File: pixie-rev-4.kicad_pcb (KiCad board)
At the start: 4 copper layers, 40 x 30 mm, 42 parts, among them J1 THD_FPC_24, SW1 SW_tact_52x52, SW2 SW_tact_52x52, SW3 SW_tact_52x52, SW4 SW_tact_52x52, U1 USBLC6-2SC6, U2 W25Q128JVS, U3 SPX3819M5-L-3-3, U4 ESP32_C3, Y2 Crystal_GND24

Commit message: Check-in before trying ESP32-C3-F4.
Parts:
- U4: footprint Package_DFN_QFN:HVQFN-32-1EP_5x5mm_P0.5mm_EP3.1x3.1mm -> Package_DFN_QFN:QFN-32-1EP_5x5mm_P0.5mm_EP3.7x3.7mm
- moved C16 1.17 mm to (152.5, 54.3)
- moved C12 0.78 mm to (154.8, 63.5)
- moved C15 0.78 mm to (154.8, 62.8)
- moved L1 0.78 mm to (156.0, 63.1)
- moved C10 0.77 mm to (156.8, 63.1)
- moved C11 0.47 mm to (152.8, 62.0)
- moved C14 0.47 mm to (152.4, 63.2)
- moved L2 0.47 mm to (153.2, 63.2)
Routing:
- net GND: track 38.5 -> 40.7 mm, vias 30 -> 64
- net Net-(U4-XTAL_N): track 8.19 -> 8.91 mm
- net Net-(AE1-Pad1): track 2.35 -> 1.83 mm
- added copper zone on F.Cu, net GND

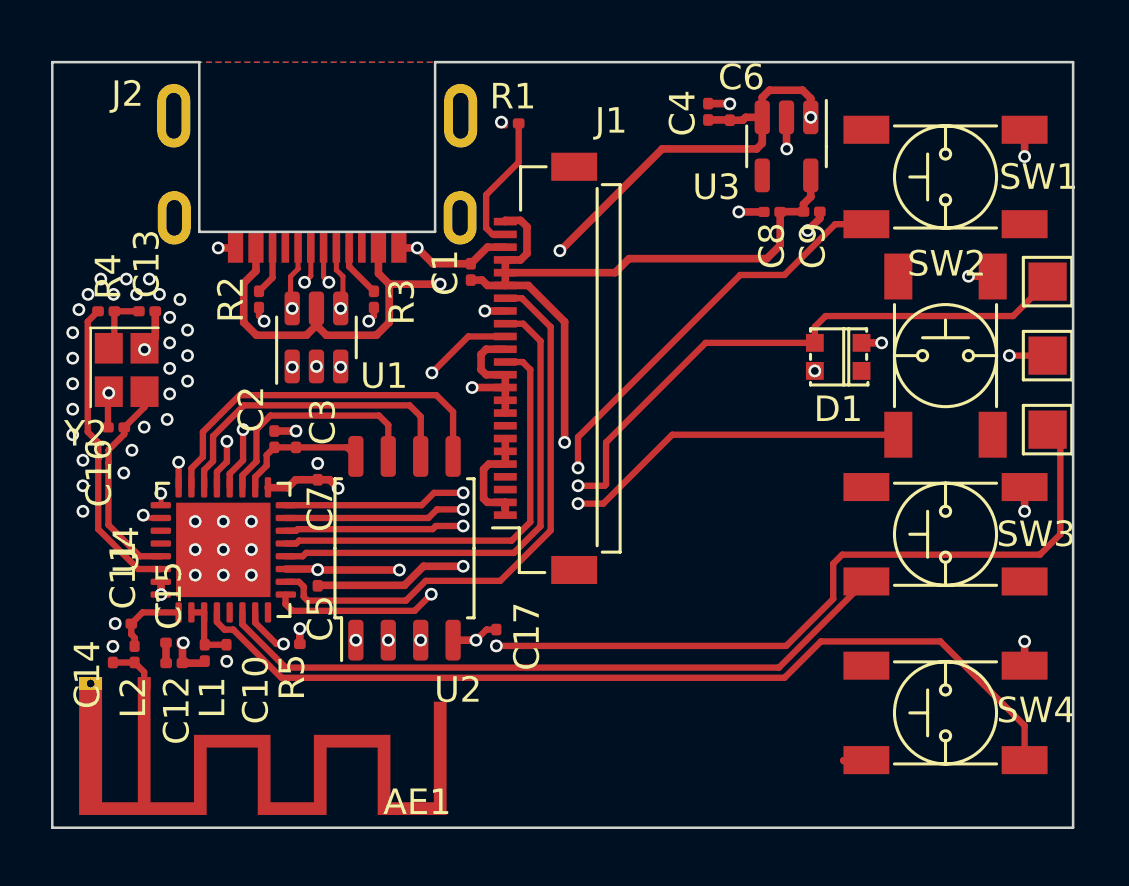
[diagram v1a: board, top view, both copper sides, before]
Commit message: Checking in before updating against ESP32-C3-WROOM-02 designs.
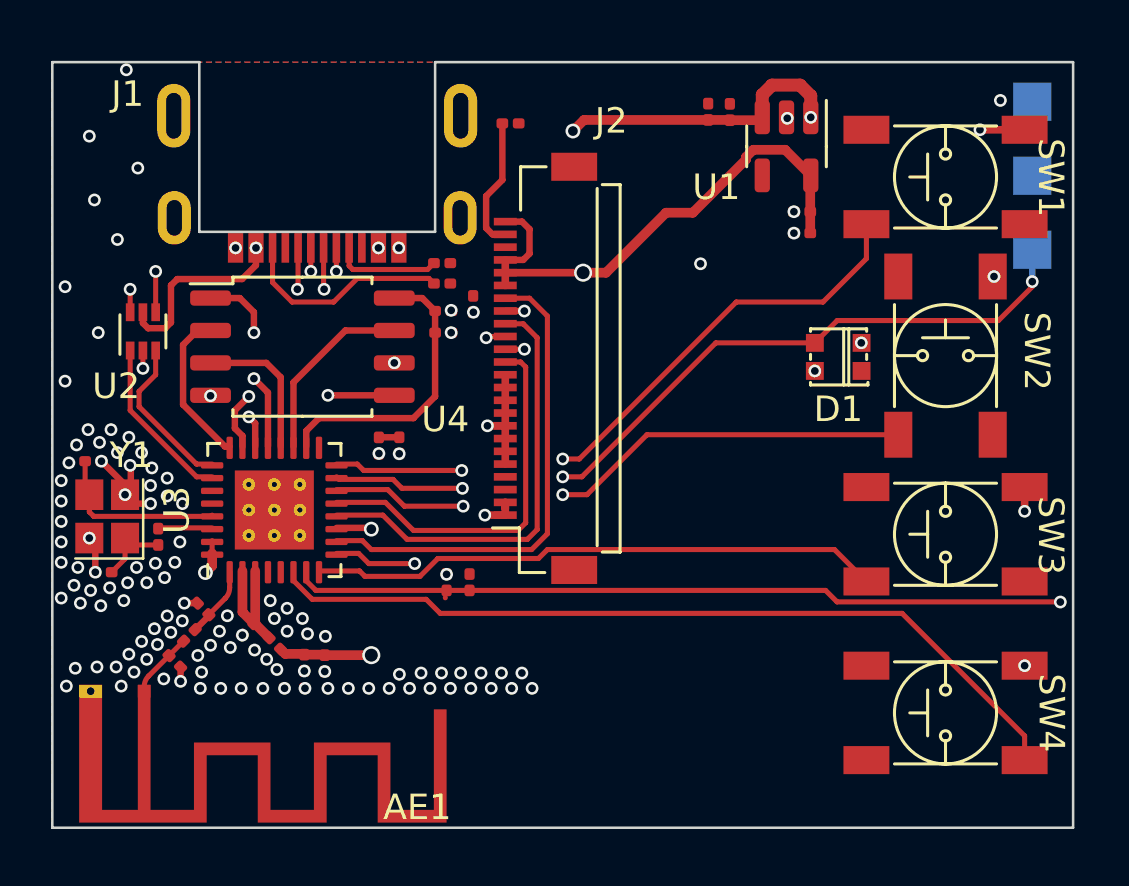
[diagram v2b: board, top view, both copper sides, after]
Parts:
- removed the C2 at (158.7, 54.8)
- removed the C3 at (159.6, 54.8)
- removed the U1 at (160.3, 50.8)
- added C16: 100n, Capacitor_SMD:C_0201_0603Metric, F.Cu at (165.3, 50.6)
- added C17: 10u, Capacitor_SMD:C_0201_0603Metric, F.Cu at (165.3, 49.8)
- added U3: ESP32-C3, Package_DFN_QFN:QFN-32-1EP_5x5mm_P0.5mm_EP3.1x3.1mm_ThermalVias, F.Cu at (158.7, 57.5)
- BOOT1, GND1, PU1: moved to B.Cu
- U2: value W25Q128JVS -> USBLC6-2SC6; footprint Package_SO:SOIC-8_5.23x5.23mm_P1.27mm -> Package_TO_SOT_SMD:SOT-563
- U4: value ESP32_C3 -> W25Q128JVS; footprint Package_DFN_QFN:QFN-32-1EP_5x5mm_P0.5mm_EP3.7x3.7mm -> Package_SO:SOIC-8_5.23x5.23mm_P1.27mm
- moved U2 13.3 mm to (153.6, 50.5)
- moved PU1 12.9 mm to (188.4, 41.5)
- moved C14 10.4 mm to (152.0, 60.0), turned to 180 degrees
- moved R5 9.07 mm to (154.2, 58.6), turned to -90 degrees
- moved U4 8.54 mm to (159.8, 51.1), turned to 0 degrees
- moved R2 7.38 mm to (166.3, 60.4), turned to 90 degrees
- moved R1 7.20 mm to (165.3, 48.7), turned to 180 degrees
- moved GND1 7.08 mm to (188.4, 44.5)
- moved C2 6.09 mm to (163.6, 55.0)
- moved C15 5.96 mm to (160.7, 63.6), turned to -90 degrees
- moved Y1 5.79 mm to (152.2, 57.8), turned to 90 degrees
- moved C13 5.10 mm to (159.9, 63.5), turned to -90 degrees
- moved C9 3.19 mm to (155.9, 61.4), turned to 135 degrees
- moved R3 3.03 mm to (165.3, 47.9), turned to 180 degrees
- moved C6 2.92 mm to (165.4, 60.4)
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- renumbered C4 to C1, C16 to C11, C14 to C12, C12 to C13, C13 to C14, C5 to C2, C6 to C3, C7 to C4, C8 to C5, C17 to C6, C9 to C7, C1 to C8, C11 to C9, J2 to J1, J1 to J2, L2 to L1, L1 to L2, R2 to R1, R5 to R2, R1 to R4, R4 to R5, U3 to U1, Y2 to Y1
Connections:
- C11 pad 1: Net-(U4-XTAL_N) -> /XTAL_N
- C9 pad 1: Net-(U4-LNA_IN) -> /ANTENNA
- L1 pad 1: Net-(U4-LNA_IN) -> /ANTENNA
- R5 pad 1: Net-(U4-XTAL_P) -> /XTAL_P
- U2 pad 1: Net-(U2-~{CS}) -> /MCU_USB_P
- U2 pad 2: Net-(U2-DO(IO1)) -> GND
- U2 pad 3: Net-(U2-IO2) -> /MCU_USB_N
- U2 pad 4: GND -> /USB_D-
- U2 pad 5: Net-(U2-DI(IO0)) -> /VBUS
- U2 pad 6: Net-(U2-CLK) -> /USB_D+
- U4 pad 1: Net-(U4-LNA_IN) -> /SPI_CS0
- U4 pad 2: /VRF -> /SPI_Q
- U4 pad 3: /VRF -> /SPI_WP
- U4 pad 4: /SW_4 -> GND
- U4 pad 5: unconnected-(U4-XTAL_32K_N_IO1-Pad5) -> /SPI_D
- U4 pad 6: /SW_3 -> /SPI_CLK
- U4 pad 7: /CHIP_PU -> /SPI_HD
- U4 pad 8: unconnected-(U4-IO3-Pad8) -> /VCC_SPI
- Y1 pad 3: Net-(U4-XTAL_N) -> /XTAL_N
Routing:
- net GND: track 40.7 -> 17.9 mm, vias 64 -> 130
- net Net-(U2-DI(IO0)): track 14.8 -> 0.00 mm
- net Net-(U2-IO2): track 13.6 -> 0.00 mm, vias 2 -> 0
- net Net-(U2-DO(IO1)): track 12.9 -> 0.00 mm, vias 2 -> 0
- net Net-(U2-CLK): track 12.5 -> 0.00 mm
- net Net-(U2-~{CS}): track 12.0 -> 0.00 mm, vias 2 -> 0
- net Net-(U4-XTAL_P): track 12.0 -> 0.00 mm
- net /CHIP_PU: track 39.5 -> 51.4 mm
- net /VCC_SPI: track 0.00 -> 11.4 mm
- net Net-(U2-IO3): track 9.28 -> 0.00 mm
- net Net-(U4-XTAL_N): track 8.91 -> 0.00 mm
- net /SPI_D: track 0.00 -> 8.03 mm, vias 0 -> 2
- net /SPI_CLK: track 0.00 -> 7.85 mm, vias 0 -> 2
- net /SPI_CS0: track 0.00 -> 7.42 mm, vias 0 -> 2
- net /SPI_HD: track 0.00 -> 7.31 mm
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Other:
- board text added: "BOOT"
- board text added: "GND"
- board text added: "RESET"
- board text added: "rev.3"
- board text removed: "rev-4u1"

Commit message: JLCPCB Submit
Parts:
- removed AE1: PCB_ANTENNA, RF_Antenna:Texas_SWRA117D_2.4GHz_Left
- removed BOOT1, GND1, PU1: TestPoint, TestPoint:TestPoint_Pad_1.5x1.5mm
- removed C1, C15, C17, C2, C7: 10u, Capacitor_SMD:C_0201_0603Metric
- removed C10, C13, C16, C3, C4, C5, C6, C8: 100n, Capacitor_SMD:C_0201_0603Metric
- removed C11, C14: 10p, Capacitor_SMD:C_0201_0603Metric
- removed C12, C9: 3p3, Capacitor_SMD:C_0201_0603Metric
- removed D1: WS2812B, firefly:WS2812B
- removed J1: ~, firefly:USB_C_SINK
- removed J2: THD_FPC_24, firefly:THD_FPC_24
- removed L1, L2: 2n2, Inductor_SMD:L_0201_0603Metric
- removed R1: 5K1 (1%), Resistor_SMD:R_0201_0603Metric
- removed R2: 5k1, Resistor_SMD:R_0201_0603Metric
- removed R3: 5k1 (1%), Resistor_SMD:R_0201_0603Metric
- removed R4: 10R, Resistor_SMD:R_0201_0603Metric
- removed R5: 22R, Resistor_SMD:R_0201_0603Metric
- removed SW1, SW2, SW3, SW4: SW_tact_52x52, firefly:SW_tact_52x52
- removed U1: SPX3819M5-L-3-3, Package_TO_SOT_SMD:SOT-23-5
- removed U2: USBLC6-2SC6, Package_TO_SOT_SMD:SOT-563
- removed U3: ESP32-C3, Package_DFN_QFN:QFN-32-1EP_5x5mm_P0.5mm_EP3.1x3.1mm_ThermalVias
- removed U4: W25Q128JVS, Package_SO:SOIC-8_5.23x5.23mm_P1.27mm
- removed Y1: Crystal_GND24, firefly:Crystal_SeikoEpson_FA20H
- added AE301: PCB_ANTENNA, firefly:PCB_Antenna, F.Cu at (153.6, 64.5)
- added BOOT301: TestPoint, TestPoint:TestPoint_Pad_1.5x1.5mm, B.Cu at (187.8, 42.2)
- added C201: 10u, Capacitor_SMD:C_0402_1005Metric, F.Cu at (176.2, 41.6)
- added C202: 100n, Capacitor_SMD:C_0201_0603Metric, F.Cu at (176.4, 42.5)
- added C203: 100n, Capacitor_SMD:C_0201_0603Metric, F.Cu at (178.3, 46.0)
- added C204: 10u, Capacitor_SMD:C_0402_1005Metric, F.Cu at (179.7, 45.8)
- added C301: 3p3, Capacitor_SMD:C_0201_0603Metric, F.Cu at (155.7, 60.2)
- added C302: 10p, Capacitor_SMD:C_0201_0603Metric, F.Cu at (151.9, 54.5)
- added C303: 100n, Capacitor_SMD:C_0201_0603Metric, F.Cu at (168.2, 61.4)
- added C304: 3p3, Capacitor_SMD:C_0201_0603Metric, F.Cu at (156.3, 62.4)
- added C305: 10p, Capacitor_SMD:C_0201_0603Metric, F.Cu at (152.3, 58.9)
- added C306: 1u, Capacitor_SMD:C_0201_0603Metric, F.Cu at (162.3, 51.0)
- added C307: 100n, Capacitor_SMD:C_0201_0603Metric, F.Cu at (157.2, 60.5)
- added C308: 1u, Capacitor_SMD:C_0201_0603Metric, F.Cu at (153.9, 59.5)
- added C309: 100n, Capacitor_SMD:C_0201_0603Metric, F.Cu at (159.7, 61.7)
- added C310: 10n, Capacitor_SMD:C_0201_0603Metric, F.Cu at (153.4, 60.3)
- added C311: 100n, Capacitor_SMD:C_0201_0603Metric, F.Cu at (160.2, 60.5)
- added C312: 100n, Capacitor_SMD:C_0201_0603Metric, F.Cu at (160.6, 52.3)
- added C313: 10u, Capacitor_SMD:C_0402_1005Metric, F.Cu at (160.6, 61.9)
- added C401: 100n, Capacitor_SMD:C_0201_0603Metric, F.Cu at (166.4, 48.6)
- added D401: WS2812B, firefly:WS2812B, F.Cu at (180.9, 52.2)
- added GND201: TestPoint, TestPoint:TestPoint_Pad_1.5x1.5mm, B.Cu at (187.7, 44.9)
- added J401: ~, firefly:THD_FPC_24, F.Cu at (169.0, 52.0)
- added L301: 2n2, Inductor_SMD:L_0201_0603Metric, F.Cu at (156.0, 61.3)
- added L302: 2n2, Inductor_SMD:L_0201_0603Metric, F.Cu at (158.2, 61.0)
- added PU301: TestPoint, TestPoint:TestPoint_Pad_1.5x1.5mm, B.Cu at (187.8, 47.5)
- added R201: 5K1, Resistor_SMD:R_0201_0603Metric, F.Cu at (155.4, 49.1)
- added R202: 5k1, Resistor_SMD:R_0201_0603Metric, F.Cu at (163.4, 49.2)
- added R301: 5k1, Resistor_SMD:R_0201_0603Metric, F.Cu at (166.6, 61.4)
- added R302: 22R, Resistor_SMD:R_0201_0603Metric, F.Cu at (154.2, 57.6)
- added R303: 0R, Resistor_SMD:R_0201_0603Metric, F.Cu at (158.0, 51.5)
- added R304: 100R, Resistor_SMD:R_0201_0603Metric, F.Cu at (157.2, 51.5)
- added R305: 100R, Resistor_SMD:R_0201_0603Metric, F.Cu at (155.7, 51.5)
- added R306: 100R, Resistor_SMD:R_0201_0603Metric, F.Cu at (159.5, 51.5)
- added R307: 100R, Resistor_SMD:R_0201_0603Metric, F.Cu at (156.5, 51.5)
- added R308: 100R, Resistor_SMD:R_0201_0603Metric, F.Cu at (158.7, 51.5)
- added R401: 10R, Resistor_SMD:R_0201_0603Metric, F.Cu at (168.7, 42.6)
- added SW101: SW_tact_52x52, firefly:SW_tact_52x52, F.Cu at (185.0, 44.5)
- added SW102: SW_tact_52x52, firefly:SW_tact_52x52, F.Cu at (185.0, 51.5)
- added SW103: SW_tact_52x52, firefly:SW_tact_52x52, F.Cu at (185.0, 58.5)
- added SW104: SW_tact_52x52, firefly:SW_tact_52x52, F.Cu at (185.0, 65.5)
- added U201: USBLC6-2SC6, Package_TO_SOT_SMD:SOT-563, F.Cu at (153.5, 50.0)
- added U202: SPX3819M5-L-3-3, Package_TO_SOT_SMD:SOT-23-5, F.Cu at (179.0, 43.2)
- added U301: W25Q128JVS, Package_SO:SOIC-8_5.23x5.23mm_P1.27mm, F.Cu at (163.9, 56.2)
- added U302: ESP32-C3, Package_DFN_QFN:QFN-32-1EP_5x5mm_P0.5mm_EP3.1x3.1mm, F.Cu at (157.8, 56.5)
- added U401: SN74LVC1T45DBV, Package_TO_SOT_SMD:SOT-23-6, F.Cu at (180.2, 49.1)
- added Y301: 40Mhz, firefly:Crystal_SeikoEpson_FA20H, F.Cu at (152.2, 56.7)
- added locked: ~, firefly:USB_C_SINK, F.Cu at (160.4, 40.0)
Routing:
- net 3V3: track 0.00 -> 77.5 mm, vias 0 -> 5
- net /3V3: track 63.9 -> 0.00 mm, vias 4 -> 0
- net 5V: track 0.00 -> 59.3 mm, vias 0 -> 5
- net /CHIP_PU: track 51.4 -> 0.00 mm, vias 2 -> 0
- net /VBUS: track 45.4 -> 0.00 mm, vias 5 -> 0
- net /MCU/CHIP_PU: track 0.00 -> 38.5 mm, vias 0 -> 3
- net /MCU/DISP_RST: track 0.00 -> 19.8 mm
- net /MCU/DISP_DC: track 0.00 -> 19.2 mm, vias 0 -> 2
- net /DISP_RST: track 19.1 -> 0.00 mm
- net /MCU/DISP_SCL: track 0.00 -> 18.5 mm
- net /DISP_SCL: track 17.4 -> 0.00 mm
- net /DISP_SDA: track 15.0 -> 0.00 mm
- net /MCU/FLASH_IO1: track 0.00 -> 15.0 mm, vias 0 -> 2
- net /DISP_DC: track 14.0 -> 0.00 mm, vias 2 -> 0
- net /MCU/FLASH_IO2: track 0.00 -> 13.5 mm, vias 0 -> 2
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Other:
- board text added: "rev.4"
- board text removed: "rev.3"

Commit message: Checking in before submitting rev.5 to JLCPCB.
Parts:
- removed SW101, SW102, SW103, SW104: SW_tact_52x52, firefly:SW_tact_52x52
- added 3V1: TestPoint, TestPoint:TestPoint_Pad_1.0x1.0mm, F.Cu at (121.2, 93.0)
- added 5V1: TestPoint, TestPoint:TestPoint_Pad_1.0x1.0mm, F.Cu at (129.6, 93.0)
- added C19: 100n, Capacitor_SMD:C_0201_0603Metric, F.Cu at (125.9, 72.9)
- added C20: 100n, Capacitor_SMD:C_0201_0603Metric, F.Cu at (129.3, 74.5)
- added D2: WS2812B, firefly:WS2812B, F.Cu at (132.1, 81.5)
- added D3: WS2812B, firefly:WS2812B, F.Cu at (132.1, 88.5)
- added D4: WS2812B, firefly:WS2812B, F.Cu at (132.1, 95.5)
- added R11: 499R, Resistor_SMD:R_0201_0603Metric, F.Cu at (101.8, 81.1)
- added REF**: mouse-bite-3.5, firefly:mouse-bite-3.5, F.Cu at (100.7, 65.5)
- added REF**: mouse-bite-3.5, firefly:mouse-bite-3.5, F.Cu at (139.3, 75.5)
- added REF**: mouse-bite-3.5, firefly:mouse-bite-3.5, F.Cu at (100.7, 75.5)
- added REF**: fiducial, firefly:fiducial, F.Cu at (96.8, 129.2)
- added REF**: mouse-bite-3.5, firefly:mouse-bite-3.5, F.Cu at (158.8, 70.8)
- added REF**: fiducial, firefly:fiducial, F.Cu at (158.8, 129.2)
- added REF**: fiducial, firefly:fiducial, F.Cu at (96.8, 66.8)
- added REF**: mouse-bite-3.5, firefly:mouse-bite-3.5, F.Cu at (150.1, 99.2)
- added REF**: mouse-bite-3.5, firefly:mouse-bite-3.5, F.Cu at (100.7, 128.4)
- added REF**: mouse-bite-3.5, firefly:mouse-bite-3.5, F.Cu at (100.7, 104.5)
- added REF**: mouse-bite-3.5, firefly:mouse-bite-3.5, F.Cu at (145.9, 70.8)
- added REF**: mouse-bite-3.5, firefly:mouse-bite-3.5, F.Cu at (133.9, 70.7)
- added REF**: fiducial, firefly:fiducial, F.Cu at (158.8, 66.8)
- added REF**: mouse-bite-3.5, firefly:mouse-bite-3.5, F.Cu at (133.9, 99.3)
- added REF**: logo-pin-25-1, firefly:logo-pin-25-1, F.Cu at (149.5, 113.5)
- added SW1: ~, firefly:button-oval, F.Cu at (135.5, 74.5)
- added SW2: ~, firefly:button-oval, F.Cu at (135.5, 81.5)
- added SW3: ~, firefly:button-oval, F.Cu at (135.5, 88.5)
- added SW4: ~, firefly:button-oval, F.Cu at (135.5, 95.5)
- added TP1: TestPoint, TestPoint:TestPoint_Pad_D1.0mm, F.Cu at (102.5, 75.2)
- added TP2: TestPoint, TestPoint:TestPoint_Pad_D1.0mm, F.Cu at (102.4, 71.9)
- BOOT1: renamed from BOOT301; footprint TestPoint:TestPoint_Pad_1.5x1.5mm -> TestPoint:TestPoint_Pad_D1.0mm; moved to F.Cu
- GND1: renamed from GND201; footprint TestPoint:TestPoint_Pad_1.5x1.5mm -> TestPoint:TestPoint_Pad_1.0x1.0mm; moved to F.Cu
- PU1: renamed from PU301; footprint TestPoint:TestPoint_Pad_1.5x1.5mm -> TestPoint:TestPoint_Pad_D1.0mm; moved to F.Cu
- Y1: renamed from Y301; footprint firefly:Crystal_SeikoEpson_FA20H -> Crystal:Crystal_SMD_2520-4Pin_2.5x2.0mm
- moved PU1 85.9 mm to (114.7, 92.7), turned to 0 degrees
- moved GND1 74.2 mm to (118.4, 71.4), turned to 0 degrees
- moved C4 73.5 mm to (123.7, 93.4), turned to 90 degrees
- moved C3 73.1 mm to (122.8, 93.6), turned to 90 degrees
- moved U2 72.4 mm to (126.4, 93.0), turned to 180 degrees
- moved BOOT1 69.3 mm to (124.8, 71.4), turned to 0 degrees
- moved C2 69.0 mm to (126.7, 90.4), turned to 90 degrees
- moved C1 68.7 mm to (128.1, 90.7), turned to 0 degrees
- moved C7 63.7 mm to (112.9, 93.0), turned to 180 degrees
- moved R3 61.9 mm to (112.9, 92.2)
- moved U4 58.3 mm to (107.8, 86.5)
- moved C12 58.3 mm to (103.9, 89.5)
- moved C17 58.3 mm to (110.6, 91.9)
- moved C18 58.3 mm to (116.4, 78.6)
- moved C8 58.3 mm to (106.3, 92.4)
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- renumbered AE301 to AE1, C201 to C1, C306 to C10, C307 to C11, C308 to C12, C309 to C13, C310 to C14, C311 to C15, C312 to C16, C313 to C17, C401 to C18, C202 to C2, C203 to C3, C204 to C4, C301 to C5, C302 to C6, C303 to C7, C304 to C8, C305 to C9, D401 to D1, J401 to J2, L301 to L1, L302 to L2, R201 to R1, R308 to R10, R401 to R12, R202 to R2, R301 to R3, R302 to R4, R303 to R5, R304 to R6, R305 to R7, R306 to R8, R307 to R9, U201 to U1, U202 to U2, U301 to U3, U302 to U4, U401 to U5
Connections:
- D1 pad 1: unconnected-(D401-D0-Pad1) -> Net-(D1-D0)
- U4 pad 14: /SW_2 -> /MCU/SW_2
- U4 pad 16: /SW_1 -> /MCU/SW_1
- U4 pad 27: unconnected-(U302-U0RXD/GPIO20-Pad27) -> /MCU/IO20
- U4 pad 28: unconnected-(U302-U0TXD/GPIO21-Pad28) -> Net-(U4-U0TXD/GPIO21)
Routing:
- net /MCU/SW_1: track 0.00 -> 38.6 mm, vias 0 -> 2
- net /MCU/SW_2: track 0.00 -> 31.2 mm, vias 0 -> 2
- net /MCU/CHIP_PU: track 38.5 -> 10.9 mm, vias 3 -> 2
- net /SW_1: track 25.6 -> 0.00 mm, vias 2 -> 0
- net /SW_2: track 23.4 -> 0.00 mm, vias 2 -> 0
- net 5V: track 59.3 -> 79.9 mm, vias 5 -> 3
- net /MCU/IO20: track 0.00 -> 13.2 mm
- net /PIXEL: track 37.2 -> 26.4 mm, vias 3 -> 2
- net /MCU/IO21: track 0.00 -> 10.0 mm
- net Net-(U4-U0TXD/GPIO21): track 0.00 -> 6.63 mm, vias 0 -> 2
- net Net-(D2-D0): track 0.00 -> 5.63 mm
- net Net-(D3-D0): track 0.00 -> 5.63 mm
- net Net-(D1-D0): track 0.00 -> 5.63 mm
- net /SW_3: track 23.0 -> 28.2 mm
- net /MCU/DISP_DC: track 19.2 -> 15.4 mm
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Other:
- board size 40 x 30 mm -> 70 x 70 mm
- board text added: "1"
- board text added: "2"
- board text added: "20"
- board text added: "21"
- board text added: "3"
- board text added: "3V"
- board text added: "4"
- board text added: "5V"
- board text added: "B"
- board text added: "G"
- board text added: "JLCJLCJLCJLC"
- board text added: "R"
- board text added: "https://firefly.app"
- board text added: "rev.5"
- board text removed: "BOOT"
- board text removed: "GND"
- board text removed: "RESET"
- board text removed: "rev.4"

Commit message: JLCPCB submit
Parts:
- J2: footprint firefly:THD_FPC_24 -> firefly:JUSHUO_FPC_24
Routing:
- net GND: track 19.4 -> 17.6 mm
- net /MCU/DISP_DC: track 15.4 -> 16.8 mm
- net /MCU/DISP_RST: track 20.1 -> 21.4 mm
- net /MCU/DISP_SCL: track 18.6 -> 19.7 mm
- net Net-(J2-LEDK): track 6.58 -> 7.32 mm, vias 0 -> 2

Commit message: Updated changes for KiCAD 8.
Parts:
- REF** (x10): value mouse-bite-3.5 -> mouse-bite-5; footprint firefly:mouse-bite-3.5 -> firefly:mouse-bite-5
- branding-logo-1: value logo-15mm_1 -> logo-15mm; footprint firefly:logo-15mm_1 -> firefly:logo-15mm
- renumbered locked to J1
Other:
- outline, holes or cut-outs redrawn
- board text added: "rev.6"
- board text removed: "rev.5"
